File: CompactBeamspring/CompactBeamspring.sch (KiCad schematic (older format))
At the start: 25 parts, among them J1 BEAMSPRING CONNECTOR, J3 EXPANSION HEADER, U1 MCP4921-E, U2 LM339A, U3 74AHC595, U4 74AHC595, U5 ProMicro, U7 74AHC595

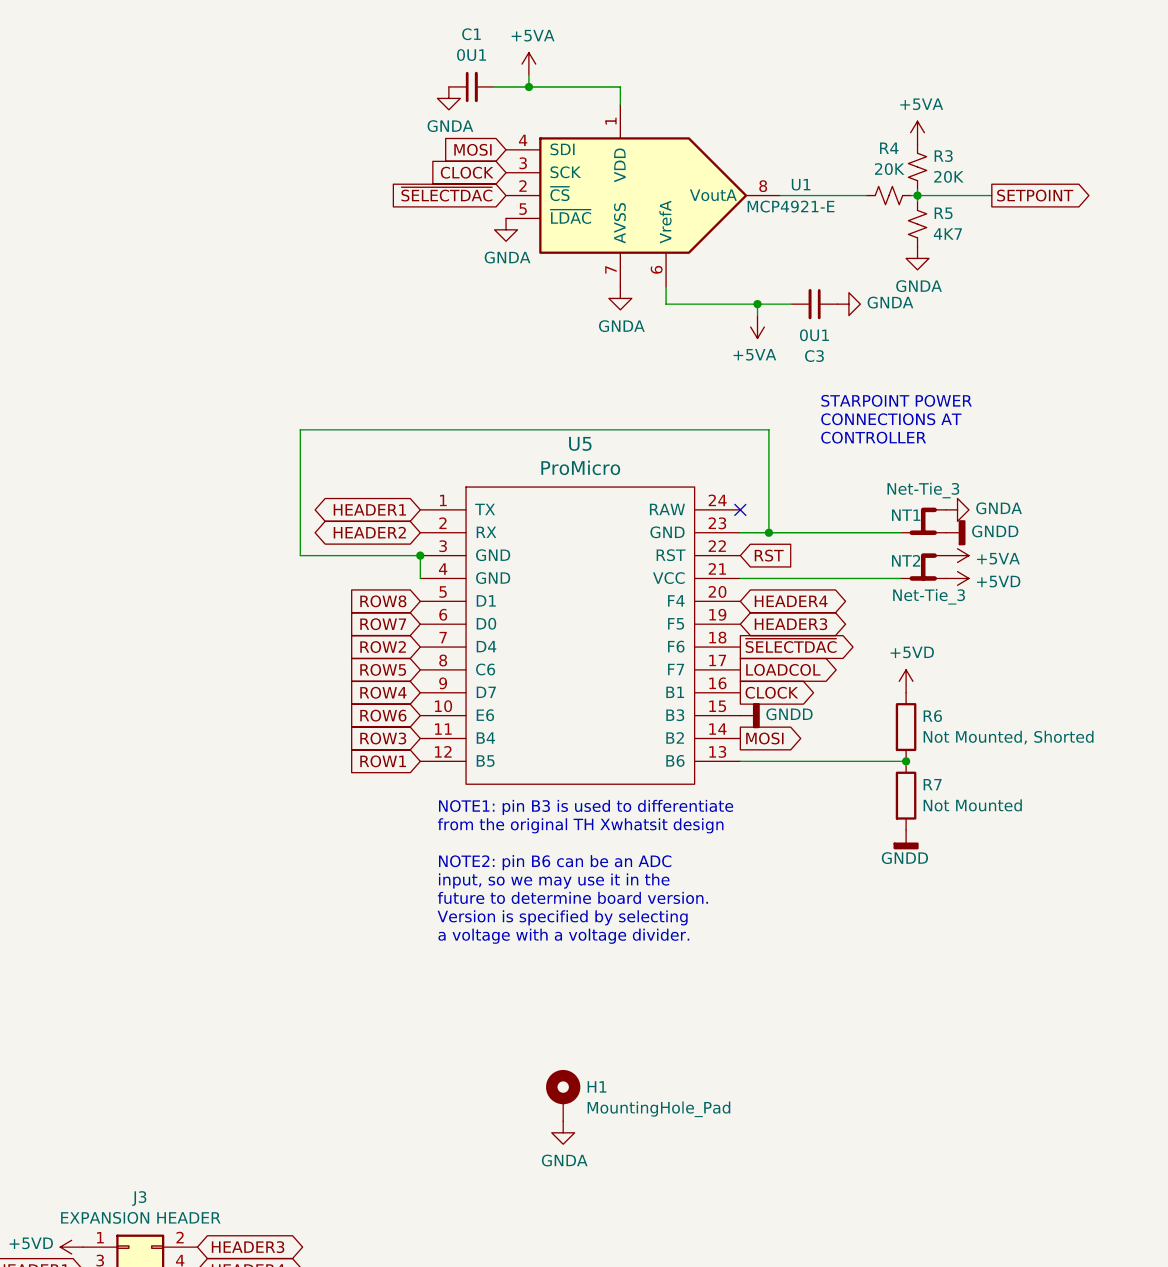
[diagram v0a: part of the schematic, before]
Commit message: made it th xwhatsit software compatible, added dac testpoints, added reset shorting pads, generally reworked to be nicer
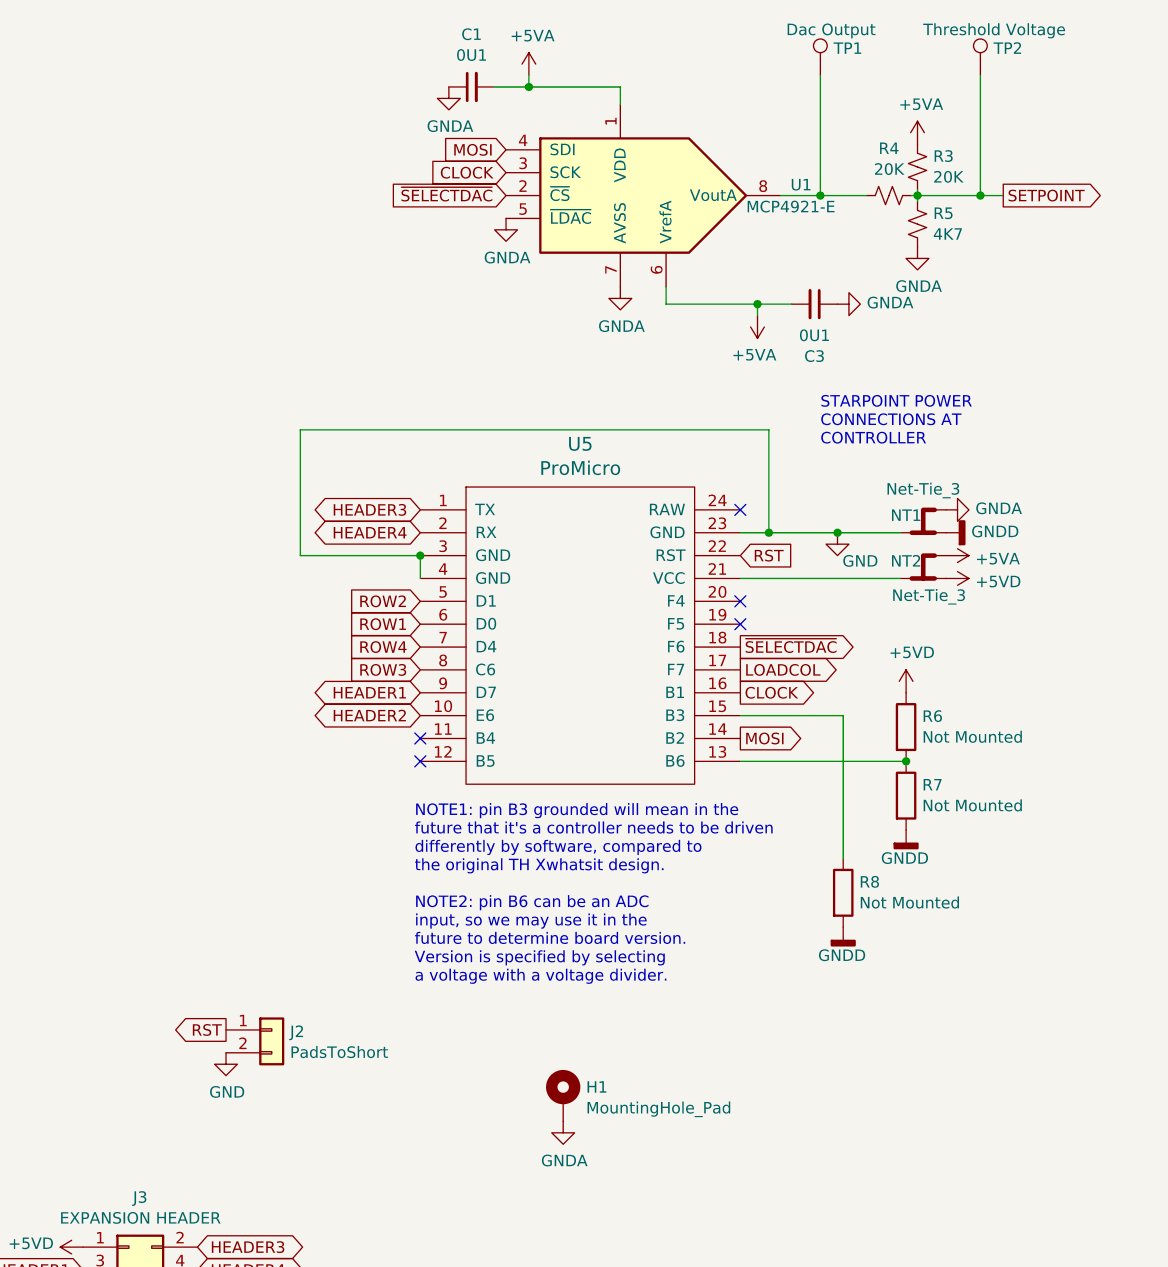
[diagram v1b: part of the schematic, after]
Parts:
- added J2: PadsToShort, TH-XWhatsIt:PadsToShort, symbol Connector_Generic:Conn_01x02
- added R8: Not Mounted, Resistor_SMD:R_0805_2012Metric_Pad1.15x1.40mm_HandSolder, symbol Device:R
- added TP1: Dac Output, TestPoint:TestPoint_Pad_D1.0mm, symbol Connector:TestPoint
- added TP2: Threshold Voltage, TestPoint:TestPoint_Pad_D1.0mm, symbol Connector:TestPoint
- R6: value Not Mounted, Shorted -> Not Mounted; footprint TH-XWhatsIt:SHORTEDR_0805_2012Metric_Pad1.15x1.40mm_HandSolder -> Resistor_SMD:R_0805_2012Metric_Pad1.15x1.40mm_HandSolder
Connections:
- net ROW5 is gone; now on net ROW3: U5.8 (C6)
- net ROW6 is gone; now on net HEADER2: U5.10 (E6)
- net ROW7 is gone; now on net ROW1: U5.6 (D0)
- net ROW8 is gone; now on net ROW2: U5.5 (D1)
- net GNDD: now also R8.2; no longer U5.15 (B3)
- net HEADER1: now also U5.9 (D7); no longer U5.1 (TX)
- net HEADER2: no longer U5.2 (RX)
- net HEADER3: now also U5.1 (TX); no longer U5.19 (F5)
- net HEADER4: now also U5.2 (RX); no longer U5.20 (F4)
- net ROW1: no longer U5.12 (B5)
- net ROW2: no longer U5.7 (D4)
- net ROW3: no longer U5.11 (B4)
- net ROW4: now also U5.7 (D4); no longer U5.9 (D7)
- net RST: now also J2.1 (Pin_1)
- net SETPOINT: now also TP2.1
- net GND: now reaches NT1.2, U5.23 (GND), U5.3 (GND), U5.4 (GND)
- net GND: now also J2.2 (Pin_2)
- net at R4.2, U1.8 (VoutA): now also TP1.1
- new net: R8.1, U5.15 (B3)
- no-connect marks 4 -> 8
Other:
- note added: "NOTE1: pin B3 grounded will mean in the\nfuture that it's a controller needs to be driven\ndifferently by software, compared to\nthe original TH Xwhatsit design.\n\nNOTE2: pin B6 can be an ADC\ninput, so we may use it in the\nfuture to determine board version.\nVersion is specified by selecting\na voltage with a voltage divider."
- note removed: "NOTE1: pin B3 is used to differentiate\nfrom the original TH Xwhatsit design\n\nNOTE2: pin B6 can be an ADC\ninput, so we may use it in the\nfuture to determine board version.\nVersion is specified by selecting\na voltage with a voltage divider."
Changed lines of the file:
@@
 encoding utf-8
 Sheet 1 1
-Title "THT-XWhatsIt combined beamspring and model f controller"
+Title "Compact Beamspring Controller Based on TH Xwhatsit"
 Date "2020-01-31"
-Rev "0.0.2"
+Rev "1.2"
 Comp "Rainy Day Plans"
 Comment1 ""
@@
 CLOCK
 NoConn ~ 9500 2775
-Text GLabel 8100 3875 0    50   Input ~ 0
+Text GLabel 8100 3275 0    50   Input ~ 0
 ROW1
+Text GLabel 8100 3175 0    50   Input ~ 0
+ROW2
+Text GLabel 8100 3475 0    50   Input ~ 0
+ROW3
 Text GLabel 8100 3375 0    50   Input ~ 0
-ROW2
-Text GLabel 8100 3775 0    50   Input ~ 0
-ROW3
-Text GLabel 8100 3575 0    50   Input ~ 0
 ROW4
-Text GLabel 8100 3475 0    50   Input ~ 0
-ROW5
-Text GLabel 8100 3675 0    50   Input ~ 0
-ROW6
-Text GLabel 8100 3275 0    50   Input ~ 0
-ROW7
-Text GLabel 8100 3175 0    50   Input ~ 0
-ROW8
 $Comp
 L 74xx:74HCT595 U4
@@
 ~SELECTDAC
 Wire Wire Line
-	9675 1400 10050 1400
+	9675 1400 9850 1400
 Wire Wire Line
 	9175 1875 9175 1800
@@
 Wire Wire Line
 	9500 3075 10200 3075
-Wire Wire Line
-	10200 2875 9625 2875
-Text Notes 9850 2500 0    50   ~ 0
-STARPOINT POWER\nCONNECTIONS AT\nCONTROLLER
 Text GLabel 2675 3875 0    50   Output ~ 0
 SENSE1
@@
 Text GLabel 7125 6100 2    50   BiDi ~ 0
 HEADER4
+Text GLabel 8100 3575 0    50   BiDi ~ 0
+HEADER1
+Text GLabel 8100 3675 0    50   BiDi ~ 0
+HEADER2
 Text GLabel 8100 2775 0    50   BiDi ~ 0
-HEADER1
+HEADER3
 Text GLabel 8100 2875 0    50   BiDi ~ 0
-HEADER2
-Text GLabel 9500 3275 2    50   BiDi ~ 0
-HEADER3
-Text GLabel 9500 3175 2    50   BiDi ~ 0
 HEADER4
 Text GLabel 6625 6200 0    50   BiDi ~ 0
@@
 Text Notes 3950 7750 0    50   ~ 0
 Copyright Rainy Day Plans.\nThis documentation describes Open Hardware and is licensed under the\nCERN OHL v. 1.2.\nYou may redistribute and modify this documentation under the terms of the\nCERN OHL v.1.2. (http://ohwr.org/cernohl). This documentation is distributed\nWITHOUT ANY EXPRESS OR IMPLIED WARRANTY, INCLUDING OF\nMERCHANTABILITY, SATISFACTORY QUALITY AND FITNESS FOR A\nPARTICULAR PURPOSE. Please see the CERN OHL v.1.2 for applicable\nconditions
-Text GLabel 10600 1400 2    50   Output ~ 0
-SETPOINT
-Wire Wire Line
-	10275 1400 10600 1400
 Text GLabel 2675 5075 0    50   Input ~ 0
 COL16
@@
 Text GLabel 5675 1175 2    50   Output ~ 0
 COL1
-$Comp
-L power:GNDD #PWR0103
-U 1 1 5F4E8027
-P 9500 3675
-F 0 "#PWR0103" H 9500 3425 50  0001 C CNN
-F 1 "GNDD" V 9504 3565 50  0000 R CNN
-F 2 "" H 9500 3675 50  0001 C CNN
-F 3 "" H 9500 3675 50  0001 C CNN
-	1    9500 3675
-	0    -1   -1   0
-$EndComp
 Wire Wire Line
 	2600 1575 3500 1575
@@
 	1    0    0    -1
 $EndComp
-Text Notes 8175 4675 0    50   ~ 0
-NOTE1: pin B3 is used to differentiate\nfrom the original TH Xwhatsit design\n\nNOTE2: pin B6 can be an ADC\ninput, so we may use it in the\nfuture to determine board version.\nVersion is specified by selecting\na voltage with a voltage divider.
+Text Notes 8075 4850 0    50   ~ 0
+NOTE1: pin B3 grounded will mean in the\nfuture that it's a controller needs to be driven\ndifferently by software, compared to\nthe original TH Xwhatsit design.\n\nNOTE2: pin B6 can be an ADC\ninput, so we may use it in the\nfuture to determine board version.\nVersion is specified by selecting\na voltage with a voltage divider.
 Text GLabel 9500 2975 2    50   Input ~ 0
 RST
@@
 P 10225 3725
 F 0 "R6" H 10295 3771 50  0000 L CNN
-F 1 "Not Mounted, Shorted" H 10295 3680 50  0000 L CNN
-F 2 "TH-XWhatsIt:SHORTEDR_0805_2012Metric_Pad1.15x1.40mm_HandSolder" V 10155 3725 50  0001 C CNN
+F 1 "Not Mounted" H 10295 3680 50  0000 L CNN
+F 2 "Resistor_SMD:R_0805_2012Metric_Pad1.15x1.40mm_HandSolder" V 10155 3725 50  0001 C CNN
 F 3 "~" H 10225 3725 50  0001 C CNN
 	1    10225 3725
@@
 	1    0    0    -1
 $EndComp
+$Comp
+L Device:R R8
+U 1 1 5F3FF7BC
+P 9950 4450
+F 0 "R8" H 10020 4496 50  0000 L CNN
+F 1 "Not Mounted" H 10020 4405 50  0000 L CNN
+F 2 "Resistor_SMD:R_0805_2012Metric_Pad1.15x1.40mm_HandSolder" V 9880 4450 50  0001 C CNN
+F 3 "~" H 9950 4450 50  0001 C CNN
+	1    9950 4450
+	1    0    0    -1
+$EndComp
+$Comp
+L power:GNDD #PWR07
+U 1 1 5F40026A
+P 9950 4600
+F 0 "#PWR07" H 9950 4350 50  0001 C CNN
+F 1 "GNDD" H 10050 4475 50  0000 R CNN
+F 2 "" H 9950 4600 50  0001 C CNN
+F 3 "" H 9950 4600 50  0001 C CNN
+	1    9950 4600
+	1    0    0    -1
+$EndComp
+Wire Wire Line
+	9950 4300 9950 3675
+Wire Wire Line
+	9950 3675 9500 3675
+NoConn ~ 9500 3175
+NoConn ~ 9500 3275
+NoConn ~ 8100 3775
+NoConn ~ 8100 3875
+$Comp
+L Connector_Generic:Conn_01x02 J2
+U 1 1 5F542CCD
+P 7450 5050
+F 0 "J2" H 7530 5042 50  0000 L CNN
+F 1 "PadsToShort" H 7530 4951 50  0000 L CNN
+F 2 "TH-XWhatsIt:PadsToShort" H 7450 5050 50  0001 C CNN
+F 3 "~" H 7450 5050 50  0001 C CNN
+	1    7450 5050
+	1    0    0    -1
+$EndComp
+Text GLabel 7250 5050 0    50   Output ~ 0
+RST
+Wire Wire Line
+	9925 2875 9625 2875
+Wire Wire Line
+	10200 2875 9925 2875
+Connection ~ 9925 2875
+$Comp
+L power:GND #PWR012
+U 1 1 5F547233
+P 9925 2875
+F 0 "#PWR012" H 9925 2625 50  0001 C CNN
+F 1 "GND" H 10025 2750 50  0000 C CNN
+F 2 "" H 9925 2875 50  0001 C CNN
+F 3 "" H 9925 2875 50  0001 C CNN
+	1    9925 2875
+	1    0    0    -1
+$EndComp
+Text Notes 9850 2500 0    50   ~ 0
+STARPOINT POWER\nCONNECTIONS AT\nCONTROLLER
+$Comp
+L power:GND #PWR08
+U 1 1 5F54D22D
+P 7250 5150
+F 0 "#PWR08" H 7250 4900 50  0001 C CNN
+F 1 "GND" H 7255 4977 50  0000 C CNN
+F 2 "" H 7250 5150 50  0001 C CNN
+F 3 "" H 7250 5150 50  0001 C CNN
+	1    7250 5150
+	1    0    0    -1
+$EndComp
+$Comp
+L Connector:TestPoint TP1
+U 1 1 5F54F052
+P 9850 875
+F 0 "TP1" H 9908 993 50  0000 L CNN
+F 1 "Dac Output" H 9700 1075 50  0000 L CNN
+F 2 "TestPoint:TestPoint_Pad_D1.0mm" H 10050 875 50  0001 C CNN
+F 3 "~" H 10050 875 50  0001 C CNN
+	1    9850 875
+	1    0    0    -1
+$EndComp
+$Comp
+L Connector:TestPoint TP2
+U 1 1 5F551CEB
+P 10550 875
+F 0 "TP2" H 10608 993 50  0000 L CNN
+F 1 "Threshold Voltage" H 10300 1075 50  0000 L CNN
+F 2 "TestPoint:TestPoint_Pad_D1.0mm" H 10750 875 50  0001 C CNN
+F 3 "~" H 10750 875 50  0001 C CNN
+	1    10550 875
+	1    0    0    -1
+$EndComp
+Wire Wire Line
+	9850 875  9850 1400
+Connection ~ 9850 1400
+Wire Wire Line
+	9850 1400 10050 1400
+Wire Wire Line
+	10550 875  10550 1400
+Connection ~ 10550 1400
+Wire Wire Line
+	10275 1400 10550 1400
+Text GLabel 10650 1400 2    50   Output ~ 0
+SETPOINT
+Wire Wire Line
+	10550 1400 10650 1400
 $EndSCHEMATC

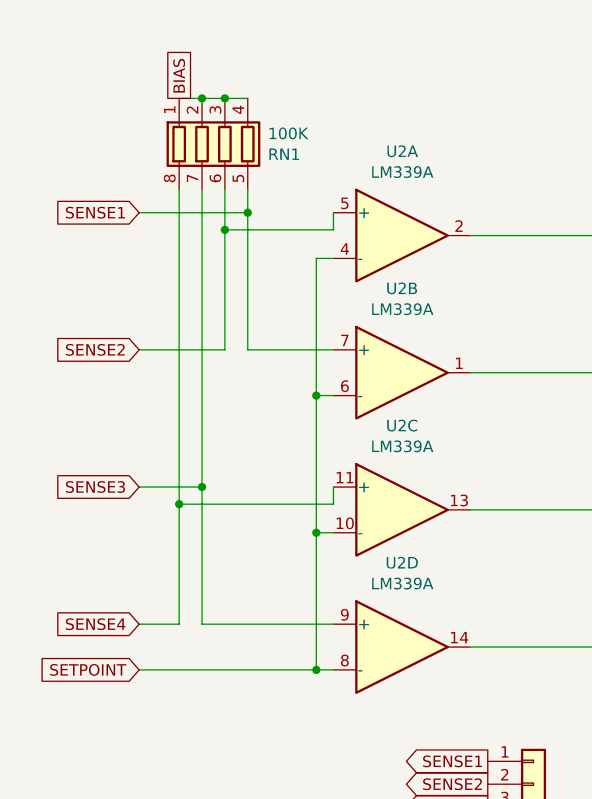
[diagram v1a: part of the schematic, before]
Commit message: Moved to individual resistors instead of resistor network, added a bit more space next to the promicro
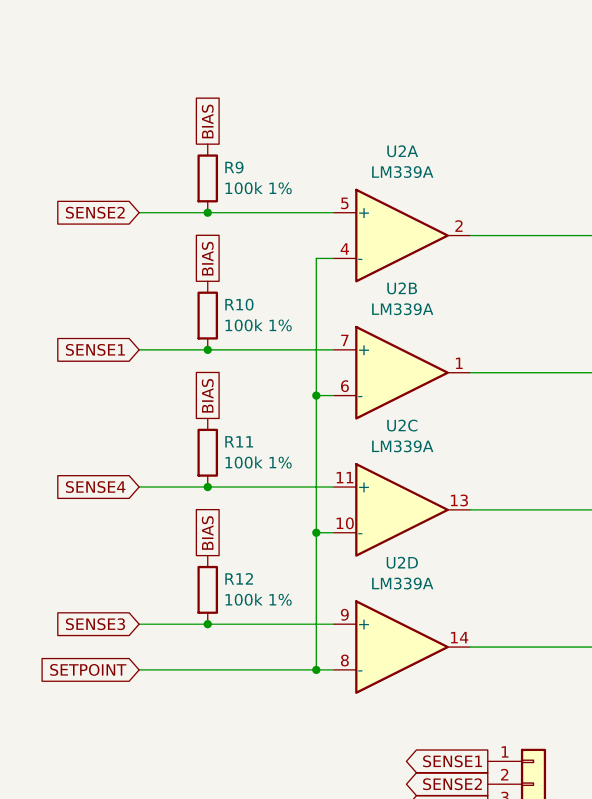
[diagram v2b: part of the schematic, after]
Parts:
- removed RN1: 100K, Resistor_SMD:R_Array_Convex_4x0603, symbol Device:R_Pack04
- added R10, R11, R12, R9: 100k 1%, Resistor_SMD:R_0805_2012Metric_Pad1.15x1.40mm_HandSolder, symbol Device:R
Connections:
- net BIAS: now also R10.1, R11.1, R12.1, R9.1
- net SENSE1: now also R10.2
- net SENSE2: now also R9.2
- net SENSE3: now also R12.2
- net SENSE4: now also R11.2
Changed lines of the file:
@@
 Title "Compact Beamspring Controller Based on TH Xwhatsit"
 Date "2020-01-31"
-Rev "1.2"
+Rev "1.3"
 Comp "Rainy Day Plans"
 Comment1 ""
@@
 $Comp
 L Comparator:LM339 U2
-U 1 1 5E3E3833
-P 2300 1575
-F 0 "U2" H 2300 1942 50  0000 C CNN
-F 1 "LM339A" H 2300 1851 50  0000 C CNN
-F 2 "Package_SO:SOIC-14_3.9x8.7mm_P1.27mm" H 2250 1675 50  0001 C CNN
-F 3 "http://www.ti.com/lit/ds/symlink/lm339.pdf" H 2350 1775 50  0001 C CNN
-F 4 "C74559" H 2300 1575 50  0001 C CNN "LCSC"
-	1    2300 1575
-	1    0    0    -1
-$EndComp
-$Comp
-L Comparator:LM339 U2
 U 2 1 5E3E3839
 P 2300 2175
@@
 	1925 3475 2000 3475
 Connection ~ 1925 2875
-Text GLabel 1150 1475 0    50   Input ~ 0
+Text GLabel 1150 2075 0    50   Input ~ 0
 SENSE1
-Text GLabel 1150 3275 0    50   Input ~ 0
-SENSE4
 Wire Wire Line
 	1925 3475 1150 3475
@@
 	0    -1   -1   0
 $EndComp
-Wire Wire Line
-	1150 1475 1625 1475
-Wire Wire Line
-	1625 1475 1625 1375
-Wire Wire Line
-	1150 2075 1525 2075
-Wire Wire Line
-	1525 2075 1525 1550
-Wire Wire Line
-	1425 1375 1425 2675
-Wire Wire Line
-	1425 2675 1150 2675
-Wire Wire Line
-	1325 1375 1325 2750
-Wire Wire Line
-	1325 3275 1150 3275
-Wire Wire Line
-	2000 2075 1625 2075
-Wire Wire Line
-	1625 2075 1625 1475
-Connection ~ 1625 1475
-Wire Wire Line
-	1525 1550 2000 1550
-Wire Wire Line
-	2000 1550 2000 1475
-Connection ~ 1525 1550
-Wire Wire Line
-	1525 1550 1525 1375
-Wire Wire Line
-	2000 3275 1425 3275
-Wire Wire Line
-	1425 3275 1425 2675
-Connection ~ 1425 2675
-Wire Wire Line
-	1325 2750 2000 2750
-Wire Wire Line
-	2000 2750 2000 2675
-Connection ~ 1325 2750
-Wire Wire Line
-	1325 2750 1325 3275
 $Comp
 L power:GNDA #PWR014
@@
 COL15
 $Comp
-L Device:R_Pack04 RN1
-U 1 1 5F34F20A
-P 1525 1175
-F 0 "RN1" H 1713 1221 50  0000 L CNN
-F 1 "100K" H 1713 1130 50  0000 L CNN
-F 2 "Resistor_SMD:R_Array_Convex_4x0603" V 1800 1175 50  0001 C CNN
-F 3 "~" H 1525 1175 50  0001 C CNN
-F 4 "C173315" H 1525 1175 50  0001 C CNN "LCSC"
-	1    1525 1175
-	1    0    0    1
-$EndComp
-Wire Wire Line
-	1325 975  1425 975
-Connection ~ 1425 975
-Wire Wire Line
-	1425 975  1525 975
-Connection ~ 1525 975
-Wire Wire Line
-	1525 975  1625 975
-$Comp
 L power:GNDA #PWR0101
 U 1 1 5F3AA298
@@
 	1    0    0    -1
 $EndComp
-Text GLabel 1325 975  1    50   UnSpc ~ 0
-BIAS
 Wire Wire Line
 	4350 6225 4350 6250
@@
 Wire Wire Line
 	2600 3375 3500 3375
-Text GLabel 1150 2675 0    50   Input ~ 0
+Text GLabel 1150 3275 0    50   Input ~ 0
 SENSE3
-Text GLabel 1150 2075 0    50   Input ~ 0
+Text GLabel 1150 1475 0    50   Input ~ 0
 SENSE2
 $Comp
@@
 Wire Wire Line
 	10550 1400 10650 1400
+$Comp
+L Device:R R9
+U 1 1 5F3E1654
+P 1450 1325
+F 0 "R9" H 1520 1371 50  0000 L CNN
+F 1 "100k 1%" H 1520 1280 50  0000 L CNN
+F 2 "Resistor_SMD:R_0805_2012Metric_Pad1.15x1.40mm_HandSolder" V 1380 1325 50  0001 C CNN
+F 3 "~" H 1450 1325 50  0001 C CNN
+F 4 "C17407" H 1450 1325 50  0001 C CNN "LCSC"
+	1    1450 1325
+	1    0    0    -1
+$EndComp
+Text GLabel 1450 1175 1    50   UnSpc ~ 0
+BIAS
+$Comp
+L Comparator:LM339 U2
+U 1 1 5E3E3833
+P 2300 1575
+F 0 "U2" H 2300 1942 50  0000 C CNN
+F 1 "LM339A" H 2300 1851 50  0000 C CNN
+F 2 "Package_SO:SOIC-14_3.9x8.7mm_P1.27mm" H 2250 1675 50  0001 C CNN
+F 3 "http://www.ti.com/lit/ds/symlink/lm339.pdf" H 2350 1775 50  0001 C CNN
+F 4 "C74559" H 2300 1575 50  0001 C CNN "LCSC"
+	1    2300 1575
+	1    0    0    -1
+$EndComp
+Wire Wire Line
+	1150 1475 1450 1475
+$Comp
+L Device:R R10
+U 1 1 5F3FE715
+P 1450 1925
+F 0 "R10" H 1520 1971 50  0000 L CNN
+F 1 "100k 1%" H 1520 1880 50  0000 L CNN
+F 2 "Resistor_SMD:R_0805_2012Metric_Pad1.15x1.40mm_HandSolder" V 1380 1925 50  0001 C CNN
+F 3 "~" H 1450 1925 50  0001 C CNN
+F 4 "C17407" H 1450 1925 50  0001 C CNN "LCSC"
+	1    1450 1925
+	1    0    0    -1
+$EndComp
+Text GLabel 1450 1775 1    50   UnSpc ~ 0
+BIAS
+Wire Wire Line
+	1150 2075 1450 2075
+Text GLabel 1150 2675 0    50   Input ~ 0
+SENSE4
+Wire Wire Line
+	1150 3275 1450 3275
+$Comp
+L Device:R R11
+U 1 1 5F434C9D
+P 1450 2525
+F 0 "R11" H 1520 2571 50  0000 L CNN
+F 1 "100k 1%" H 1520 2480 50  0000 L CNN
+F 2 "Resistor_SMD:R_0805_2012Metric_Pad1.15x1.40mm_HandSolder" V 1380 2525 50  0001 C CNN
+F 3 "~" H 1450 2525 50  0001 C CNN
+F 4 "C17407" H 1450 2525 50  0001 C CNN "LCSC"
+	1    1450 2525
+	1    0    0    -1
+$EndComp
+Text GLabel 1450 2375 1    50   UnSpc ~ 0
+BIAS
+$Comp
+L Device:R R12
+U 1 1 5F43B7B4
+P 1450 3125
+F 0 "R12" H 1520 3171 50  0000 L CNN
+F 1 "100k 1%" H 1520 3080 50  0000 L CNN
+F 2 "Resistor_SMD:R_0805_2012Metric_Pad1.15x1.40mm_HandSolder" V 1380 3125 50  0001 C CNN
+F 3 "~" H 1450 3125 50  0001 C CNN
+F 4 "C17407" H 1450 3125 50  0001 C CNN "LCSC"
+	1    1450 3125
+	1    0    0    -1
+$EndComp
+Text GLabel 1450 2975 1    50   UnSpc ~ 0
+BIAS
+Connection ~ 1450 1475
+Wire Wire Line
+	1450 1475 2000 1475
+Connection ~ 1450 2075
+Wire Wire Line
+	1450 2075 2000 2075
+Connection ~ 1450 2675
+Wire Wire Line
+	1450 2675 1150 2675
+Wire Wire Line
+	1450 2675 2000 2675
+Connection ~ 1450 3275
+Wire Wire Line
+	1450 3275 2000 3275
 $EndSCHEMATC
